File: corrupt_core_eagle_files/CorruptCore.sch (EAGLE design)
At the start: 90 parts, among them K1 DTS-3, K10 DTS-3, K11 DTS-3, K12 DTS-3, K13 DTS-3, K14 DTS-3, K15 DTS-3, K16 DTS-3, K2 DTS-3, K3 DTS-3, K4 DTS-3, K5 DTS-3, K6 DTS-3, K7 DTS-3, K8 DTS-3, K9 DTS-3, T1 TRANS_NPN-MMBTA42, T2 TRANS_NPN-MMBTA42, T3 TRANS_NPN-MMBTA42, T4 TRANS_NPN-MMBTA42, U1 MEGA8-P, U2 SNX4HC595SOIC16, U3 SNX4HC595SOIC16, U4 SNX4HC595SOIC16, U5 ULN2803ASOIC18, U6 ULN2803ASOIC18, U7 ULN2803ASOIC18, U8 LTC1799, Y1 16MHz

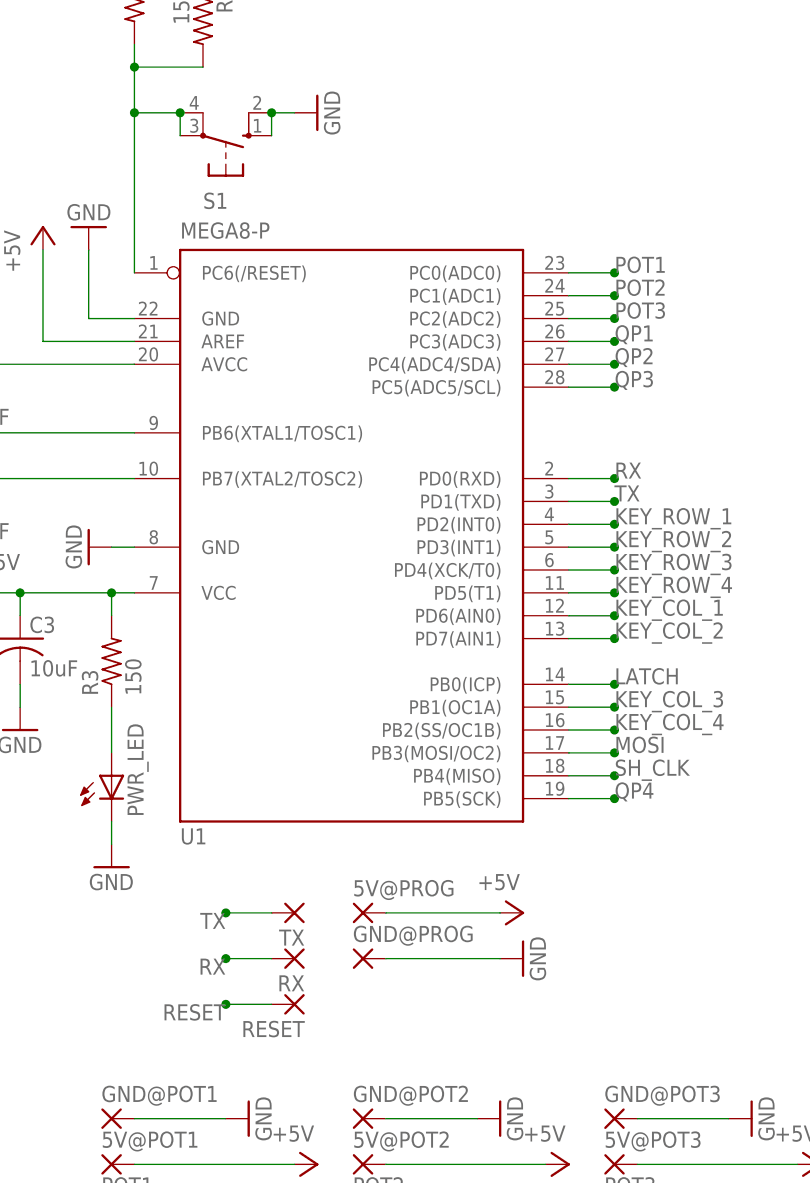
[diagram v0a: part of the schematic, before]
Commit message: -starting to fix up the soldermask
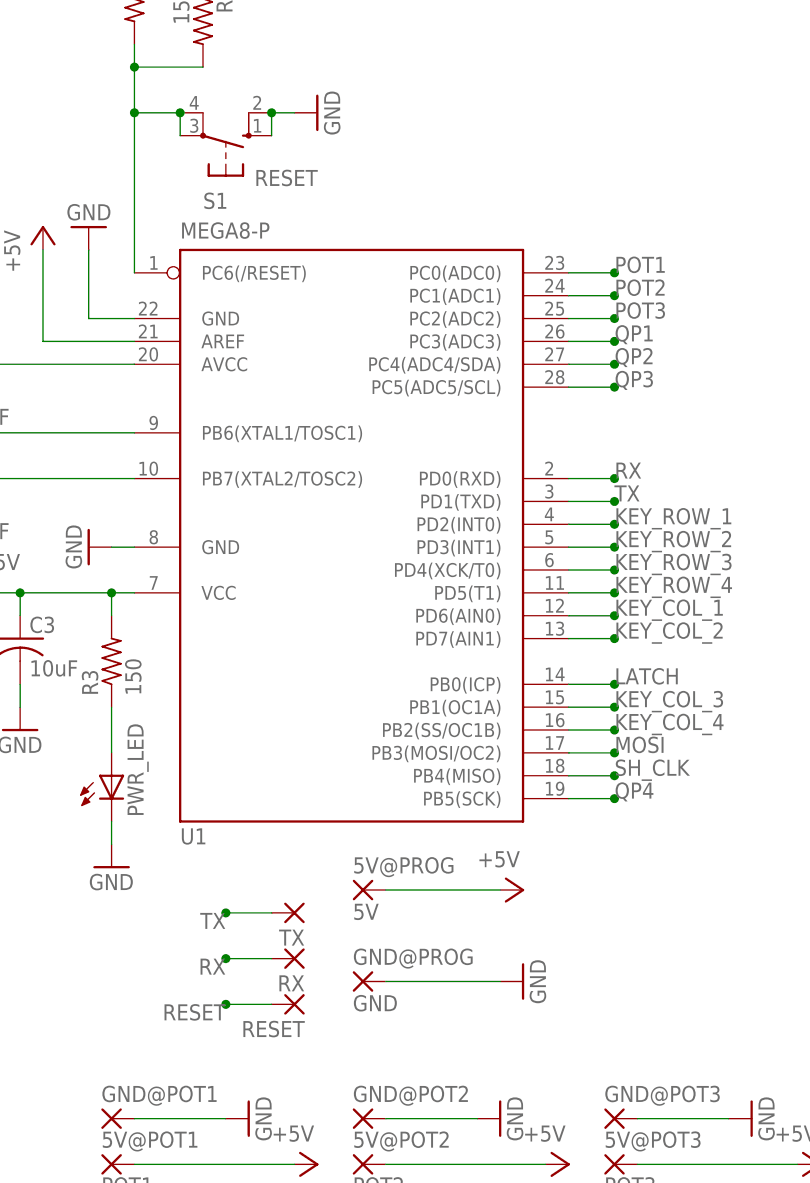
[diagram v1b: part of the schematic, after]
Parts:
- 5V@PROG: value (none) -> 5V
- GND@PROG: value (none) -> GND
- S1: value (none) -> RESET
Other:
- moved on the sheet: 5V@PROG, GND@PROG
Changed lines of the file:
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@@
 <?xml version="1.0" encoding="utf-8"?>
 <!DOCTYPE eagle SYSTEM "eagle.dtd">
-<eagle version="8.2.1">
+<eagle version="8.2.2">
 <drawing>
 <settings>
@@
 <part name="GND10" library="supply1" library_urn="urn:adsk.eagle:library:371" deviceset="GND" device=""/>
 <part name="B2_P1" library="wirepad" library_urn="urn:adsk.eagle:library:412" deviceset="1,6/0,8" device=""/>
-<part name="S1" library="switch-omron" library_urn="urn:adsk.eagle:library:377" deviceset="10-XX" device=""/>
+<part name="S1" library="switch-omron" library_urn="urn:adsk.eagle:library:377" deviceset="10-XX" device="" value="RESET"/>
 <part name="GND11" library="supply1" library_urn="urn:adsk.eagle:library:371" deviceset="GND" device=""/>
 <part name="U4" library="CorruptCore" deviceset="SNX4HC595" device="SOIC16"/>
@@
 <part name="RX" library="wirepad" library_urn="urn:adsk.eagle:library:412" deviceset="1,6/0,8" device=""/>
 <part name="RESET" library="wirepad" library_urn="urn:adsk.eagle:library:412" deviceset="1,6/0,8" device=""/>
-<part name="5V@PROG" library="wirepad" library_urn="urn:adsk.eagle:library:412" deviceset="1,6/0,8" device=""/>
-<part name="GND@PROG" library="wirepad" library_urn="urn:adsk.eagle:library:412" deviceset="1,6/0,8" device=""/>
+<part name="5V@PROG" library="wirepad" library_urn="urn:adsk.eagle:library:412" deviceset="1,6/0,8" device="" value="5V"/>
+<part name="GND@PROG" library="wirepad" library_urn="urn:adsk.eagle:library:412" deviceset="1,6/0,8" device="" value="GND"/>
 <part name="GND35" library="supply1" library_urn="urn:adsk.eagle:library:371" deviceset="GND" device=""/>
 <part name="P+11" library="supply1" library_urn="urn:adsk.eagle:library:371" deviceset="+5V" device=""/>
@@
 <instance part="RX" gate="P" x="35.56" y="-38.1" rot="R180"/>
 <instance part="RESET" gate="P" x="35.56" y="-43.18" rot="R180"/>
-<instance part="5V@PROG" gate="P" x="43.18" y="-33.02"/>
-<instance part="GND@PROG" gate="P" x="43.18" y="-38.1"/>
-<instance part="GND35" gate="1" x="60.96" y="-38.1" rot="R90"/>
-<instance part="P+11" gate="1" x="60.96" y="-33.02" rot="R270"/>
+<instance part="5V@PROG" gate="P" x="43.18" y="-30.48"/>
+<instance part="GND@PROG" gate="P" x="43.18" y="-40.64"/>
+<instance part="GND35" gate="1" x="60.96" y="-40.64" rot="R90"/>
+<instance part="P+11" gate="1" x="60.96" y="-30.48" rot="R270"/>
 <instance part="GND@POT1" gate="P" x="15.24" y="-55.88"/>
 <instance part="5V@POT1" gate="P" x="15.24" y="-60.96"/>
@@
 <segment>
 <pinref part="5V@PROG" gate="P" pin="P"/>
-<wire x1="45.72" y1="-33.02" x2="58.42" y2="-33.02" width="0.1524" layer="91"/>
+<wire x1="45.72" y1="-30.48" x2="58.42" y2="-30.48" width="0.1524" layer="91"/>
 <pinref part="P+11" gate="1" pin="+5V"/>
 </segment>
@@
 <segment>
 <pinref part="GND@PROG" gate="P" pin="P"/>
-<wire x1="45.72" y1="-38.1" x2="58.42" y2="-38.1" width="0.1524" layer="91"/>
+<wire x1="45.72" y1="-40.64" x2="58.42" y2="-40.64" width="0.1524" layer="91"/>
 <pinref part="GND35" gate="1" pin="GND"/>
 </segment>

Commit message: -more silkscreen changes
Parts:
- renumbered 5V@FREQ to 5V@CLK, FP1 to CPT1, FP2 to CPT2, FREQ to CLK_OUT, FREQSET to CLKSET, GND@FREQ to GND@CLK
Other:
- moved on the sheet: B1_P1, B1_P2, B1_P3, B1_P4, B1_P5, B1_P6, B1_P7, B1_P8
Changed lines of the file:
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@@
 <part name="P+15" library="supply1" library_urn="urn:adsk.eagle:library:371" deviceset="+5V" device=""/>
 <part name="GND15" library="supply1" library_urn="urn:adsk.eagle:library:371" deviceset="GND" device=""/>
-<part name="FREQ" library="wirepad" library_urn="urn:adsk.eagle:library:412" deviceset="1,6/0,8" device=""/>
+<part name="CLK_OUT" library="wirepad" library_urn="urn:adsk.eagle:library:412" deviceset="1,6/0,8" device=""/>
 <part name="DIV" library="wirepad" library_urn="urn:adsk.eagle:library:412" deviceset="1,6/0,8" device=""/>
-<part name="5V@FREQ" library="wirepad" library_urn="urn:adsk.eagle:library:412" deviceset="1,6/0,8" device=""/>
-<part name="GND@FREQ" library="wirepad" library_urn="urn:adsk.eagle:library:412" deviceset="1,6/0,8" device=""/>
+<part name="5V@CLK" library="wirepad" library_urn="urn:adsk.eagle:library:412" deviceset="1,6/0,8" device=""/>
+<part name="GND@CLK" library="wirepad" library_urn="urn:adsk.eagle:library:412" deviceset="1,6/0,8" device=""/>
 <part name="P+16" library="supply1" library_urn="urn:adsk.eagle:library:371" deviceset="+5V" device=""/>
 <part name="GND16" library="supply1" library_urn="urn:adsk.eagle:library:371" deviceset="GND" device=""/>
-<part name="FREQSET" library="resistor" library_urn="urn:adsk.eagle:library:348" deviceset="R-US_" device="0207/7" value="user"/>
+<part name="CLKSET" library="resistor" library_urn="urn:adsk.eagle:library:348" deviceset="R-US_" device="0207/7" value="user"/>
 <part name="C5" library="resistor" library_urn="urn:adsk.eagle:library:348" deviceset="C-US" device="C0805" value="100nF"/>
-<part name="FP2" library="wirepad" library_urn="urn:adsk.eagle:library:412" deviceset="1,6/0,8" device=""/>
-<part name="FP1" library="wirepad" library_urn="urn:adsk.eagle:library:412" deviceset="1,6/0,8" device=""/>
+<part name="CPT2" library="wirepad" library_urn="urn:adsk.eagle:library:412" deviceset="1,6/0,8" device=""/>
+<part name="CPT1" library="wirepad" library_urn="urn:adsk.eagle:library:412" deviceset="1,6/0,8" device=""/>
 <part name="P+17" library="supply1" library_urn="urn:adsk.eagle:library:371" deviceset="+5V" device=""/>
 </parts>
@@
 <instance part="U5" gate="G$1" x="220.98" y="53.34"/>
 <instance part="GND7" gate="1" x="193.04" y="33.02" rot="R270"/>
-<instance part="B1_P1" gate="P" x="248.92" y="73.66" rot="R180"/>
+<instance part="B1_P1" gate="P" x="251.46" y="73.66" rot="R180"/>
 <instance part="U3" gate="G$1" x="139.7" y="2.54"/>
 <instance part="GND8" gate="1" x="109.22" y="-15.24" rot="R270"/>
@@
 <instance part="GND14" gate="1" x="193.04" y="-73.66" rot="R270"/>
 <instance part="B3_P1" gate="P" x="251.46" y="-33.02" rot="R180"/>
-<instance part="B1_P2" gate="P" x="248.92" y="68.58" rot="R180"/>
-<instance part="B1_P3" gate="P" x="248.92" y="63.5" rot="R180"/>
-<instance part="B1_P4" gate="P" x="248.92" y="58.42" rot="R180"/>
-<instance part="B1_P5" gate="P" x="248.92" y="53.34" rot="R180"/>
-<instance part="B1_P6" gate="P" x="248.92" y="48.26" rot="R180"/>
-<instance part="B1_P7" gate="P" x="248.92" y="43.18" rot="R180"/>
-<instance part="B1_P8" gate="P" x="248.92" y="38.1" rot="R180"/>
+<instance part="B1_P2" gate="P" x="251.46" y="68.58" rot="R180"/>
+<instance part="B1_P3" gate="P" x="251.46" y="63.5" rot="R180"/>
+<instance part="B1_P4" gate="P" x="251.46" y="58.42" rot="R180"/>
+<instance part="B1_P5" gate="P" x="251.46" y="53.34" rot="R180"/>
+<instance part="B1_P6" gate="P" x="251.46" y="48.26" rot="R180"/>
+<instance part="B1_P7" gate="P" x="251.46" y="43.18" rot="R180"/>
+<instance part="B1_P8" gate="P" x="251.46" y="38.1" rot="R180"/>
 <instance part="B2_P2" gate="P" x="251.46" y="15.24" rot="R180"/>
 <instance part="B2_P3" gate="P" x="251.46" y="10.16" rot="R180"/>
@@
 <instance part="P+15" gate="1" x="330.2" y="5.08" rot="MR0"/>
 <instance part="GND15" gate="1" x="317.5" y="5.08" rot="MR180"/>
-<instance part="FREQ" gate="P" x="373.38" y="-7.62" rot="MR0"/>
+<instance part="CLK_OUT" gate="P" x="373.38" y="-7.62" rot="MR0"/>
 <instance part="DIV" gate="P" x="373.38" y="-17.78" rot="MR0"/>
-<instance part="5V@FREQ" gate="P" x="345.44" y="-33.02"/>
-<instance part="GND@FREQ" gate="P" x="345.44" y="-27.94"/>
+<instance part="5V@CLK" gate="P" x="345.44" y="-33.02"/>
+<instance part="GND@CLK" gate="P" x="345.44" y="-27.94"/>
 <instance part="P+16" gate="1" x="358.14" y="-33.02" rot="MR90"/>
 <instance part="GND16" gate="1" x="360.68" y="-27.94" rot="MR270"/>
-<instance part="FREQSET" gate="G$1" x="330.2" y="-27.94" rot="R90"/>
+<instance part="CLKSET" gate="G$1" x="330.2" y="-27.94" rot="R90"/>
 <instance part="C5" gate="G$1" x="325.12" y="0" rot="R270"/>
-<instance part="FP2" gate="P" x="330.2" y="-38.1" rot="R90"/>
-<instance part="FP1" gate="P" x="330.2" y="-43.18" rot="R270"/>
+<instance part="CPT2" gate="P" x="330.2" y="-38.1" rot="R90"/>
+<instance part="CPT1" gate="P" x="330.2" y="-43.18" rot="R270"/>
 <instance part="P+17" gate="1" x="330.2" y="-50.8" rot="MR180"/>
 </instances>
@@
 </segment>
 <segment>
-<pinref part="5V@FREQ" gate="P" pin="P"/>
+<pinref part="5V@CLK" gate="P" pin="P"/>
 <pinref part="P+16" gate="1" pin="+5V"/>
 <wire x1="347.98" y1="-33.02" x2="355.6" y2="-33.02" width="0.1524" layer="91"/>
@@
 </segment>
 <segment>
-<pinref part="FP1" gate="P" pin="P"/>
+<pinref part="CPT1" gate="P" pin="P"/>
 <wire x1="330.2" y1="-45.72" x2="330.2" y2="-48.26" width="0.1524" layer="91"/>
 <pinref part="P+17" gate="1" pin="+5V"/>
@@
 </segment>
 <segment>
-<pinref part="GND@FREQ" gate="P" pin="P"/>
+<pinref part="GND@CLK" gate="P" pin="P"/>
 <pinref part="GND16" gate="1" pin="GND"/>
 <wire x1="347.98" y1="-27.94" x2="358.14" y2="-27.94" width="0.1524" layer="91"/>
@@
 <segment>
 <pinref part="U5" gate="G$1" pin="1C"/>
-<wire x1="231.14" y1="73.66" x2="246.38" y2="73.66" width="0.1524" layer="91"/>
+<wire x1="231.14" y1="73.66" x2="248.92" y2="73.66" width="0.1524" layer="91"/>
 <pinref part="B1_P1" gate="P" pin="P"/>
 </segment>
@@
 <segment>
 <pinref part="U5" gate="G$1" pin="2C"/>
-<wire x1="231.14" y1="68.58" x2="246.38" y2="68.58" width="0.1524" layer="91"/>
+<wire x1="231.14" y1="68.58" x2="248.92" y2="68.58" width="0.1524" layer="91"/>
 <pinref part="B1_P2" gate="P" pin="P"/>
 </segment>
@@
 <segment>
 <pinref part="U5" gate="G$1" pin="3C"/>
-<wire x1="231.14" y1="63.5" x2="246.38" y2="63.5" width="0.1524" layer="91"/>
+<wire x1="231.14" y1="63.5" x2="248.92" y2="63.5" width="0.1524" layer="91"/>
 <pinref part="B1_P3" gate="P" pin="P"/>
 </segment>
@@
 <segment>
 <pinref part="U5" gate="G$1" pin="4C"/>
-<wire x1="231.14" y1="58.42" x2="246.38" y2="58.42" width="0.1524" layer="91"/>
+<wire x1="231.14" y1="58.42" x2="248.92" y2="58.42" width="0.1524" layer="91"/>
 <pinref part="B1_P4" gate="P" pin="P"/>
 </segment>
@@
 <segment>
 <pinref part="U5" gate="G$1" pin="5C"/>
-<wire x1="231.14" y1="53.34" x2="246.38" y2="53.34" width="0.1524" layer="91"/>
+<wire x1="231.14" y1="53.34" x2="248.92" y2="53.34" width="0.1524" layer="91"/>
 <pinref part="B1_P5" gate="P" pin="P"/>
 </segment>
@@
 <segment>
 <pinref part="U5" gate="G$1" pin="6C"/>
-<wire x1="231.14" y1="48.26" x2="246.38" y2="48.26" width="0.1524" layer="91"/>
+<wire x1="231.14" y1="48.26" x2="248.92" y2="48.26" width="0.1524" layer="91"/>
 <pinref part="B1_P6" gate="P" pin="P"/>
 </segment>
@@
 <segment>
 <pinref part="U5" gate="G$1" pin="7C"/>
-<wire x1="231.14" y1="43.18" x2="246.38" y2="43.18" width="0.1524" layer="91"/>
+<wire x1="231.14" y1="43.18" x2="248.92" y2="43.18" width="0.1524" layer="91"/>
 <pinref part="B1_P7" gate="P" pin="P"/>
 </segment>
@@
 <segment>
 <pinref part="U5" gate="G$1" pin="8C"/>
-<wire x1="231.14" y1="38.1" x2="246.38" y2="38.1" width="0.1524" layer="91"/>
+<wire x1="231.14" y1="38.1" x2="248.92" y2="38.1" width="0.1524" layer="91"/>
 <pinref part="B1_P8" gate="P" pin="P"/>
 </segment>
@@
 <pinref part="U8" gate="G$1" pin="OUT"/>
 <wire x1="358.14" y1="-7.62" x2="370.84" y2="-7.62" width="0.1524" layer="91"/>
-<pinref part="FREQ" gate="P" pin="P"/>
+<pinref part="CLK_OUT" gate="P" pin="P"/>
 </segment>
 </net>
@@
 <net name="N$16" class="0">
 <segment>
-<pinref part="FREQSET" gate="G$1" pin="2"/>
+<pinref part="CLKSET" gate="G$1" pin="2"/>
 <wire x1="330.2" y1="-22.86" x2="330.2" y2="-17.78" width="0.1524" layer="91"/>
 <pinref part="U8" gate="G$1" pin="SET"/>
@@
 <net name="N$14" class="0">
 <segment>
-<pinref part="FREQSET" gate="G$1" pin="1"/>
-<pinref part="FP2" gate="P" pin="P"/>
+<pinref part="CLKSET" gate="G$1" pin="1"/>
+<pinref part="CPT2" gate="P" pin="P"/>
 <wire x1="330.2" y1="-35.56" x2="330.2" y2="-33.02" width="0.1524" layer="91"/>
 </segment>

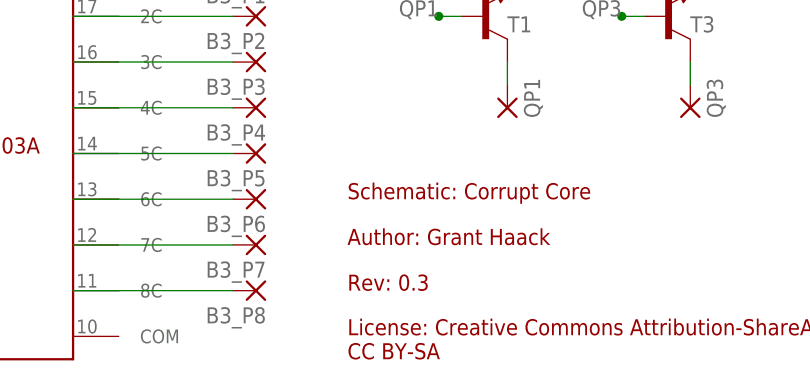
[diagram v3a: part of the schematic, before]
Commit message: -added a CSV BOM from DigiKey (I wanted to use mouser but they don't carry the LTC1799) -updated the schematic image
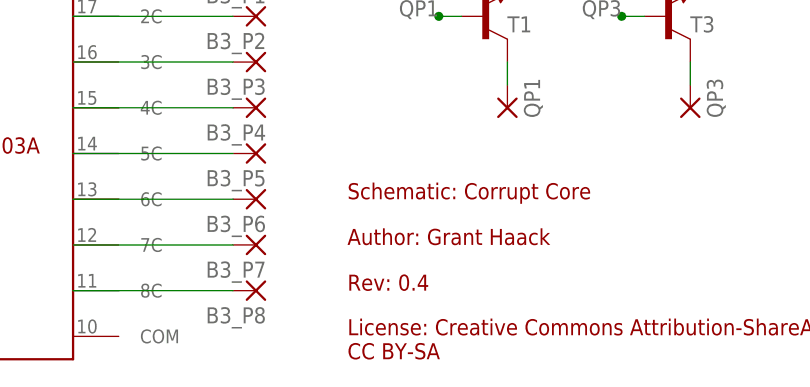
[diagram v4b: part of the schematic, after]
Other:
- note added: "Rev: 0.4"
- note removed: "Rev: 0.3"
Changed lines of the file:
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@@
 <text x="261.62" y="-58.42" size="1.778" layer="94">Schematic: Corrupt Core</text>
 <text x="261.62" y="-63.5" size="1.778" layer="94">Author: Grant Haack</text>
-<text x="261.62" y="-68.58" size="1.778" layer="94">Rev: 0.3</text>
+<text x="261.62" y="-68.58" size="1.778" layer="94">Rev: 0.4</text>
 <text x="261.62" y="-76.2" size="1.778" layer="94">License: Creative Commons Attribution-ShareAlike
 CC BY-SA</text>
